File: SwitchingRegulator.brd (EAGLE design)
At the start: 111.7 x 62.7 mm, 30 parts, among them J1 APP_2POS_CONFIG5V_HORIZ, J2 APP_2POS_CONFIG5V_HORIZ, J4 APP_2POS_CONFIG12V_HORIZ, Q2 Q_CSD18532KCSPCB, Q3 Q_CSD18532KCSPCB, U1 OKI-78SR-5/1.5-W36HC

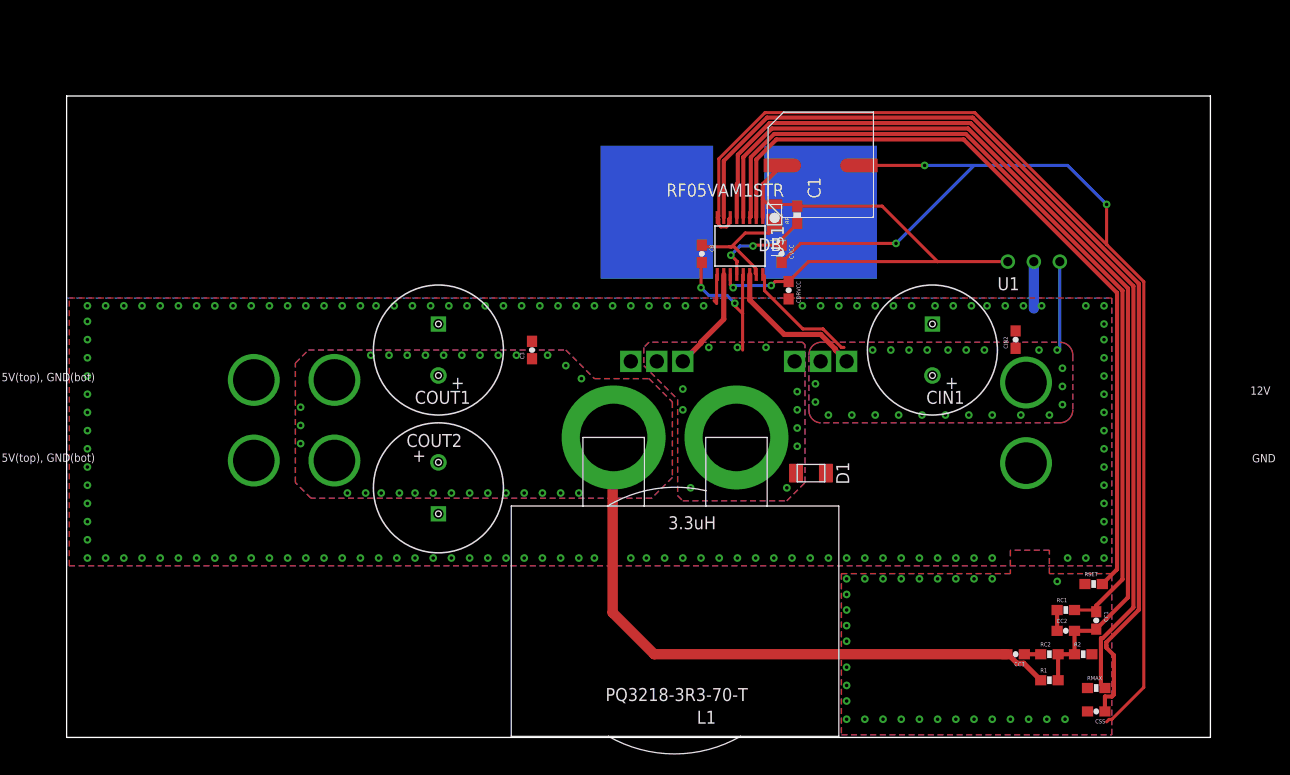
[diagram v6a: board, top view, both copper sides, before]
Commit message: Major revision, moved LTC to bottom
Changed signal traces to be much closer to LTC chip.  Modified via stitching to cover whole polygon rather than edges only.  No more vias under IC.  Moved inductor to top side of board to prevent LTC from heating up due to MOSFET heat.  Added silkscreen stuff.  More fine details to come
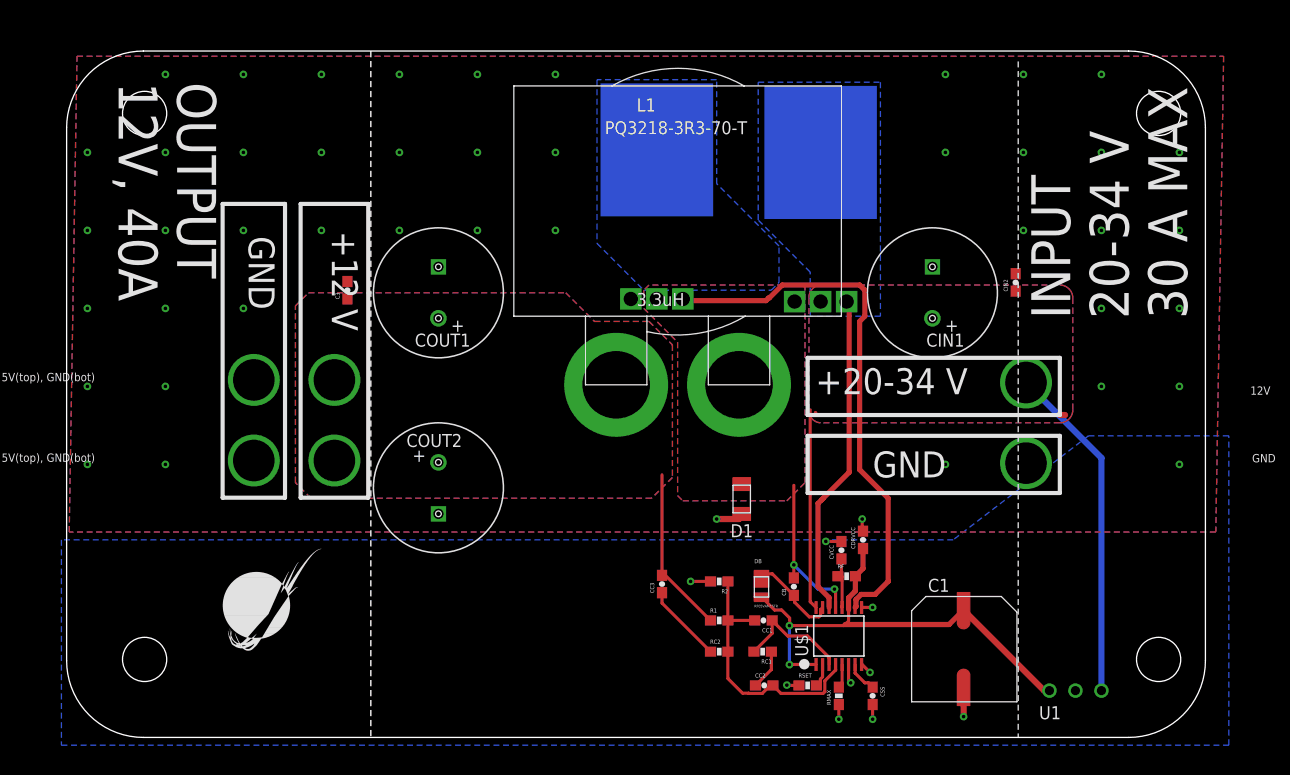
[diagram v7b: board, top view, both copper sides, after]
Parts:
- added H1, H2, H3, H4: MOUNTING_HOLE#8, MRDT-Hardware:#8_SCREW
- added LOGO1: MRDT_LOGO, MRDT-Hardware:MRDT_LOGO
- moved C1 49.3 mm to (87.6, 8.64), turned to 0 degrees
- moved U1 42.1 mm to (101.1, 4.57)
- moved U$1 39.3 mm to (75.4, 9.91), turned to 0 degrees
- moved DB 38.4 mm to (67.2, 13.7), turned to 0 degrees
- moved L1 36.8 mm to (43.7, 41.1), turned to 0 degrees
- moved R2 36.3 mm to (63.8, 15.2), turned to 180 degrees
- moved RF 35.6 mm to (76.2, 15.7), turned to 0 degrees
- moved CC3 35.2 mm to (58.2, 15.0), turned to 90 degrees
- moved CB 33.7 mm to (71.0, 14.7), turned to 90 degrees
- moved R1 32.8 mm to (63.8, 11.4)
- moved CC1 32.5 mm to (68.1, 11.4), turned to 180 degrees
- moved RC2 32.3 mm to (63.8, 8.38)
- moved CC2 29.9 mm to (68.1, 5.08)
- moved RC1 29.9 mm to (68.0, 8.38), turned to 180 degrees
- moved RSET 29.6 mm to (72.4, 5.08)
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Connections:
- net N$15 renamed 5V
- net N$17: now also L1.P$2; no longer L1.P$1
- net VOUT12+: now also L1.P$1; no longer L1.P$2
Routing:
- net GND: track 163.7 -> 18.1 mm, vias 163 -> 54
- net N$6: track 98.7 -> 3.12 mm
- net N$4: track 93.5 -> 2.34 mm
- net N$3: track 77.0 -> 2.30 mm
- net N$7: track 84.1 -> 11.5 mm
- net N$11: track 94.3 -> 26.0 mm
- net VOUT12+: track 61.7 -> 16.4 mm, vias 29 -> 0
- net N$16: track 10.1 -> 53.2 mm
- net VBATT: track 20.3 -> 53.3 mm, vias 24 -> 0
- net N$2: track 14.5 -> 31.9 mm
- net 5V: track 55.4 -> 48.8 mm
- net N$10: track 1.60 -> 7.72 mm
- net N$13: track 10.3 -> 5.37 mm, vias 2 -> 0
- net N$1: track 12.0 -> 8.75 mm
- net N$9: track 2.03 -> 3.94 mm
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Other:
- board size 111.7 x 62.7 mm -> 111.3 x 67.1 mm
- board text added: "+12 V"
- board text added: "+20-34 V"
- board text added: "GND"
- board text added: "INPUT 20-34 V 30 A MAX"
- board text added: "OUTPUT 12V, 40A"

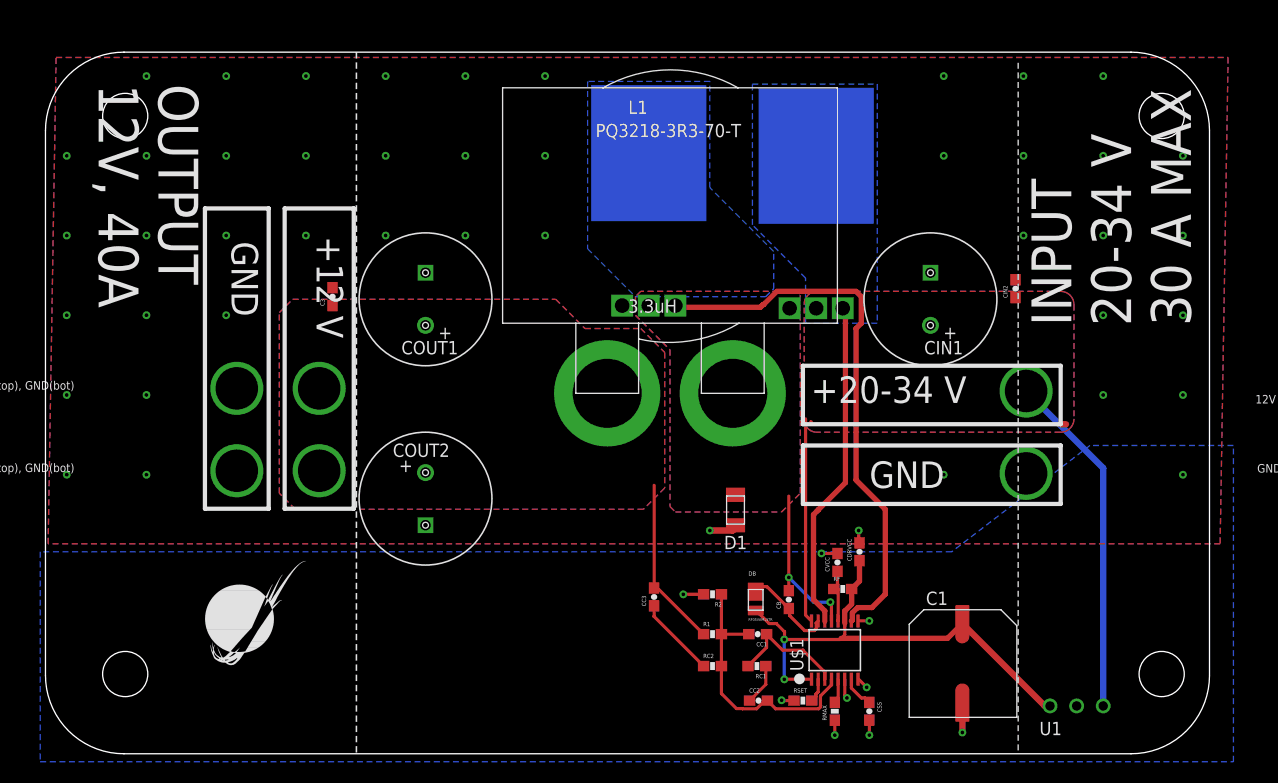
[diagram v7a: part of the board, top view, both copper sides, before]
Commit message: Finishing touches
Finished via stitching, added labels and logo, adjusted mounting holes
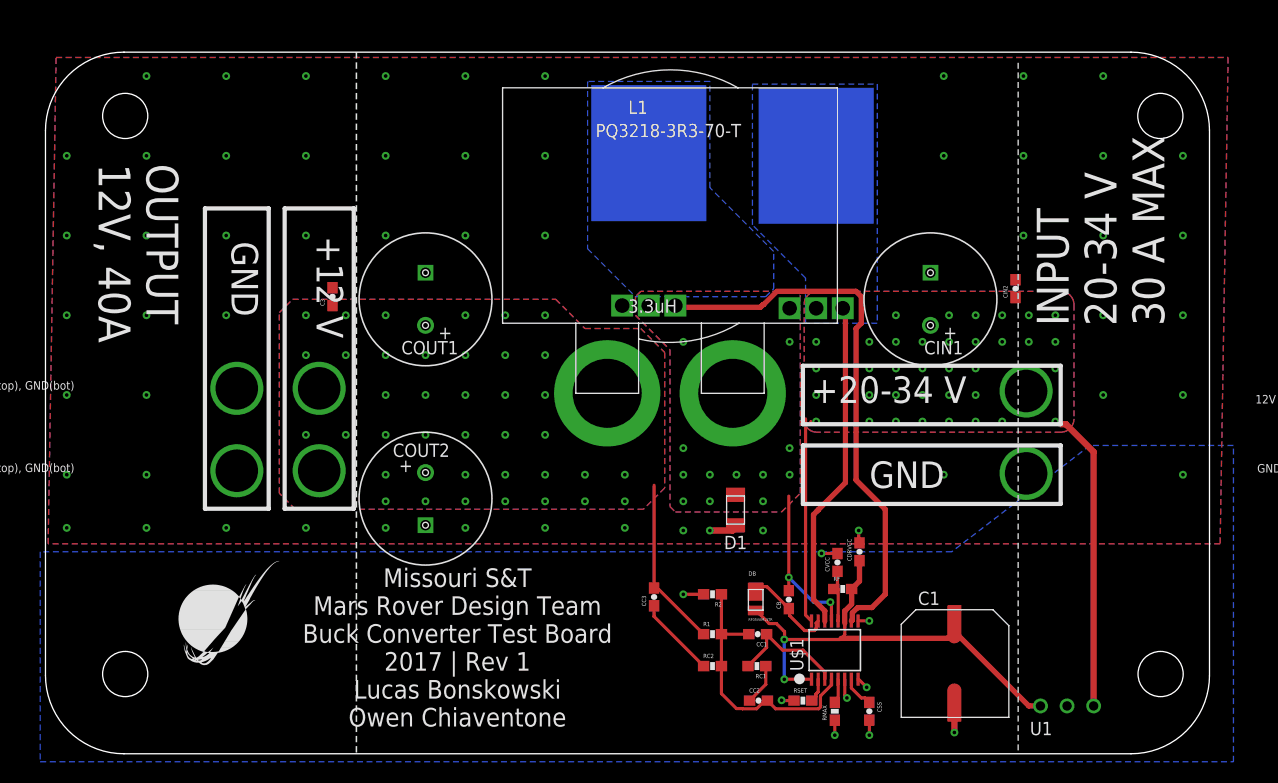
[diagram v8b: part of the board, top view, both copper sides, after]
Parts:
- moved LOGO1 2.54 mm to (12.7, 7.62)
- moved U1 0.91 mm to (100.2, 4.57)
- moved C1 0.76 mm to (86.9, 8.64)
- moved H3 0.13 mm to (106.6, 61.0)
- moved H2 0.10 mm to (106.6, 7.62)
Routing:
- net VBATT: track 53.3 -> 48.2 mm, vias 0 -> 36
- net VOUT12+: vias 0 -> 38
- net N$17: vias 2 -> 14
- net GND: vias 54 -> 64
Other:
- board text added: "Missouri S&T Mars Rover Design Team Buck Converter Test Board 2017 | Rev 1 Lucas Bonskowski Owen Chiaventone"
